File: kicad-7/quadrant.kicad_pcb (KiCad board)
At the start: 4 copper layers, 53 x 73.5 mm, 96 parts, among them J1 USB_C_Receptacle_USB2.0, J2 Conn_01x02_Male, J7 Conn_01x06, Q1 DMN601DMK-7, Q2 NCE3400, U1 VRD2833PTX, U2 W25Q128JVS, U3 VRH4801NTX, U7 DS3911, U8 TSV994IPT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

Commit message: moved component labels
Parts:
- removed C1, C2, C3: 1 uF, Capacitor_SMD:C_0805_2012Metric_Pad1.18x1.45mm_HandSolder
- removed U1: VRD2833PTX, quadrant:SOT-26
- added C25: 1 uF, Capacitor_SMD:C_0805_2012Metric_Pad1.18x1.45mm_HandSolder, F.Cu at (15.5, -50.5)
- added C26: 1 uF, Capacitor_SMD:C_0805_2012Metric_Pad1.18x1.45mm_HandSolder, F.Cu at (7.50, -49.5)
- added C40: 22nF, Capacitor_SMD:C_0805_2012Metric_Pad1.18x1.45mm_HandSolder, F.Cu at (15.5, -48.0)
- added C41: 1 uF, Capacitor_SMD:C_0805_2012Metric_Pad1.18x1.45mm_HandSolder, F.Cu at (7.00, -54.0)
- added C42: 1 uF, Capacitor_SMD:C_0805_2012Metric_Pad1.18x1.45mm_HandSolder, F.Cu at (14.0, -54.0)
- added U4: RT9193-33GB, Package_TO_SOT_SMD:SOT-23-5, F.Cu at (11.0, -49.5)
- added U5: LP5907MFX-2.8_NOPB, Package_TO_SOT_SMD:SOT-23-5, F.Cu at (10.5, -54.0)
- moved MIDI0 4.56 mm to (4.55, -9.22), turned to 180 degrees
- moved VC0 4.55 mm to (4.55, -29.0), turned to 180 degrees
- moved VC3 4.55 mm to (34.5, -4.55), turned to -90 degrees
- moved VC1 4.55 mm to (19.0, -69.0), turned to 90 degrees
- moved VC2 4.45 mm to (48.5, -44.5), turned to 0 degrees
- moved R2 1.70 mm to (3.50, -56.5)
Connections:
- J1 pad A8: Net-(J1-PadA8) -> unconnected-(J1-SBU1-PadA8)
- J1 pad B8: Net-(J1-PadB8) -> unconnected-(J1-SBU2-PadB8)
- MIDI0 pad TN: Net-(MIDI0-PadTN) -> unconnected-(MIDI0-PadTN)
- U3 pad 4: Net-(U3-Pad4) -> unconnected-(U3-NC-Pad4)
- U9 pad 11: Net-(U9-Pad11) -> unconnected-(U9-GPIO8-Pad11)
- U9 pad 12: Net-(U9-Pad12) -> unconnected-(U9-GPIO9-Pad12)
- U9 pad 13: Net-(U9-Pad13) -> unconnected-(U9-GPIO10-Pad13)
- U9 pad 18: Net-(U9-Pad18) -> unconnected-(U9-GPIO15-Pad18)
- U9 pad 19: Net-(U9-Pad19) -> unconnected-(U9-TESTEN-Pad19)
- U9 pad 21: Net-(U9-Pad21) -> unconnected-(U9-XOUT-Pad21)
- U9 pad 26: Net-(U9-Pad26) -> unconnected-(U9-RUN-Pad26)
- U9 pad 27: Net-(U9-Pad27) -> unconnected-(U9-GPIO16-Pad27)
- U9 pad 28: Net-(U9-Pad28) -> unconnected-(U9-GPIO17-Pad28)
- U9 pad 32: Net-(U9-Pad32) -> unconnected-(U9-GPIO21-Pad32)
- U9 pad 34: Net-(U9-Pad34) -> unconnected-(U9-GPIO22-Pad34)
- U9 pad 38: Net-(U9-Pad38) -> unconnected-(U9-GPIO26_ADC0-Pad38)
- U9 pad 39: Net-(U9-Pad39) -> unconnected-(U9-GPIO27_ADC1-Pad39)
- U9 pad 40: Net-(U9-Pad40) -> unconnected-(U9-GPIO28_ADC2-Pad40)
- U9 pad 41: Net-(U9-Pad41) -> unconnected-(U9-GPIO29_ADC3-Pad41)
- U9 pad 5: Net-(U9-Pad5) -> unconnected-(U9-GPIO3-Pad5)
- VC0 pad TN: Net-(VC0-PadTN) -> unconnected-(VC0-PadTN)
- VC1 pad TN: Net-(VC1-PadTN) -> unconnected-(VC1-PadTN)
- VC2 pad TN: Net-(VC2-PadTN) -> unconnected-(VC2-PadTN)
- VC3 pad TN: Net-(VC3-PadTN) -> unconnected-(VC3-PadTN)
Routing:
- net USB5V: track 121.9 -> 134.7 mm
- net +3V3: track 54.3 -> 66.7 mm
- net +2V8: track 103.7 -> 116.1 mm
- net GND: track 87.0 -> 93.6 mm, vias 21 -> 20
- net Net-(U4-BP): track 0.00 -> 2.55 mm
- net Net-(J1-CC2): track 8.34 -> 7.32 mm
- net USBD+: track 36.9 -> 36.1 mm
- net unconnected-(MIDI0-PadTN): vias 0 -> 1
- net SDA: vias 4 -> 3

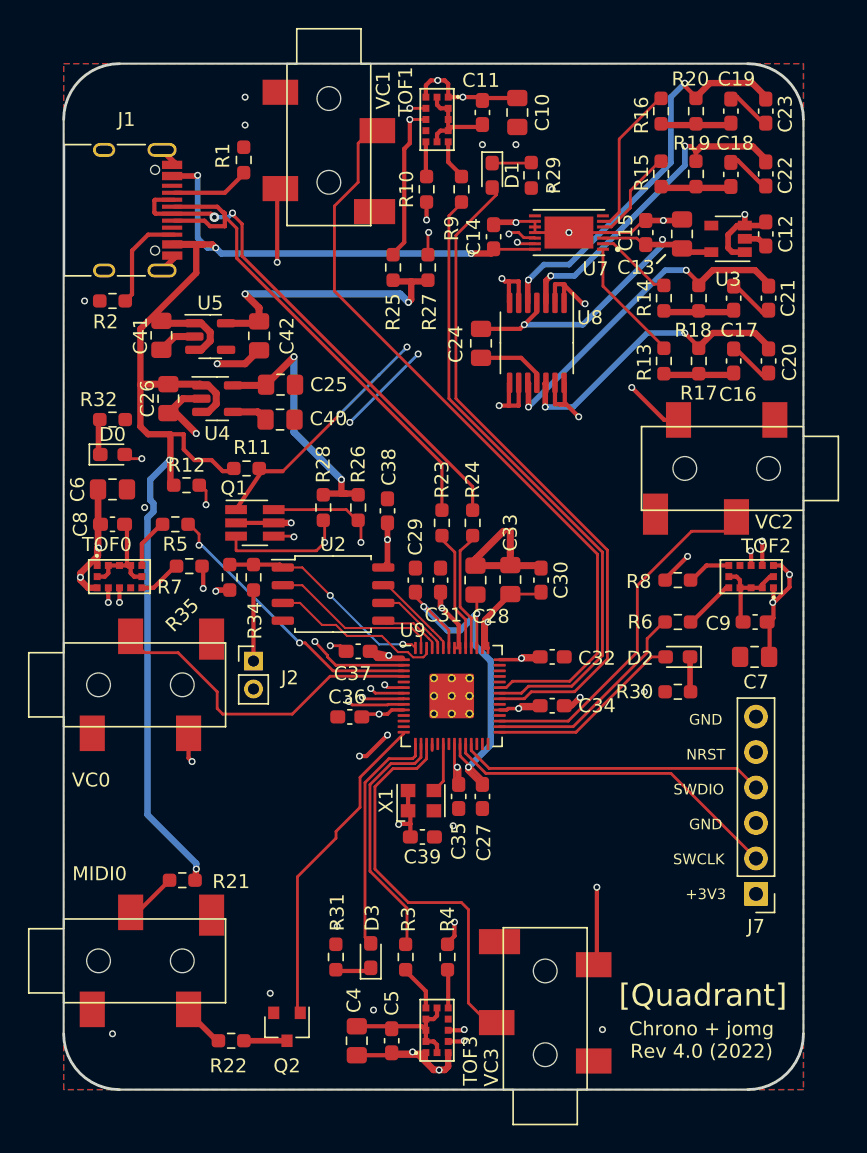
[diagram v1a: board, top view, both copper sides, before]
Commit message: change schottky diode, update pcb
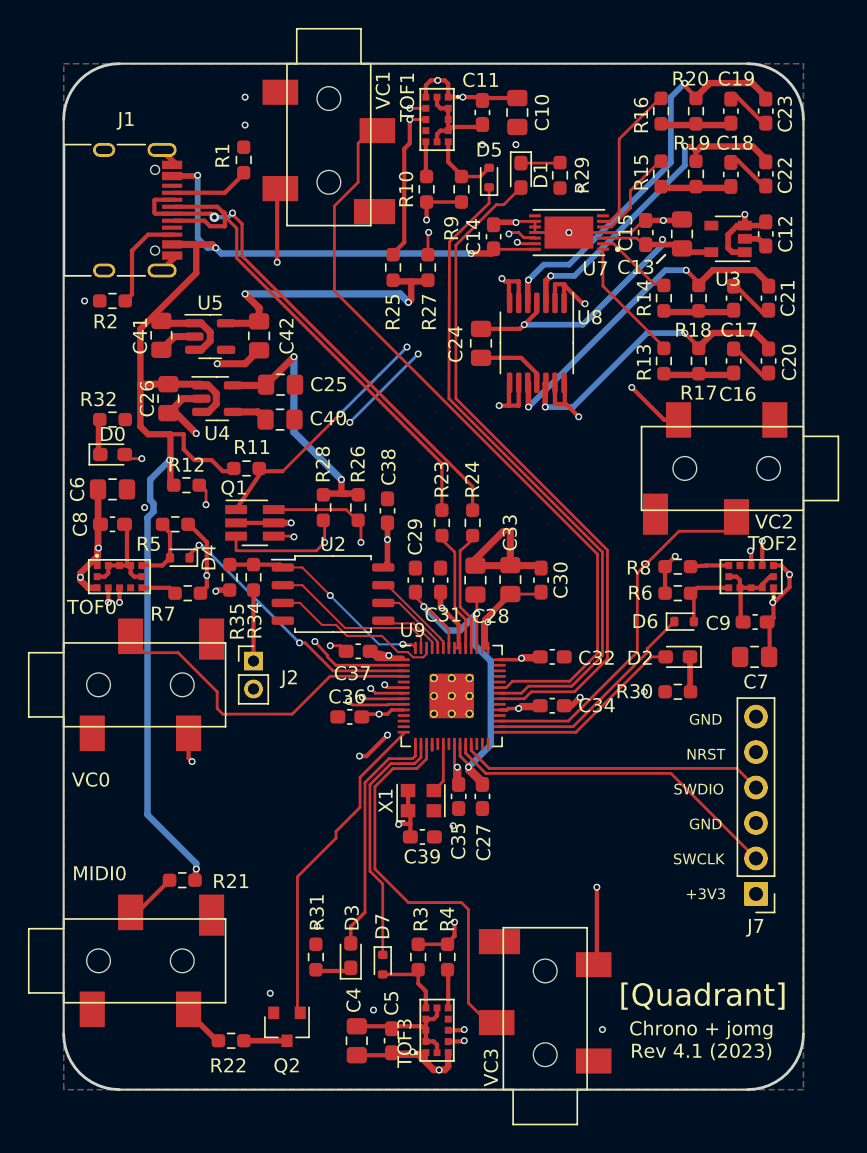
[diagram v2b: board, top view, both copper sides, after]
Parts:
- added D4: D_Schottky, Diode_SMD:D_SOD-523, F.Cu at (8.32, -38.1)
- added D5: D_Schottky, Diode_SMD:D_SOD-523, F.Cu at (30.5, -65.3)
- added D6: D_Schottky, Diode_SMD:D_SOD-523, F.Cu at (44.5, -33.5)
- added D7: D_Schottky, Diode_SMD:D_SOD-523, F.Cu at (22.9, -8.95)
- VC0, VC1, VC2, VC3: value AudioJack2_Ground_SwitchT -> PJ-327C-4A
- moved R29 2.06 mm to (35.6, -65.5)
- moved R6 2.06 mm to (44.0, -35.6)
- moved D1 2.06 mm to (32.8, -65.5)
- moved R7 1.94 mm to (8.89, -35.6)
- moved D3 1.43 mm to (20.6, -9.60)
- moved R31 1.43 mm to (18.1, -9.50)
- moved R8 0.97 mm to (44.0, -37.5)
- moved R3 0.90 mm to (25.4, -9.50)
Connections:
- R3 pad 1: EN3 -> +2V8
- R5 pad 1: EN0 -> +2V8
- R6 pad 1: EN2 -> +2V8
- R9 pad 1: EN1 -> +2V8
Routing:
- net +2V8: track 116.1 -> 125.8 mm
- net Net-(D7-A): track 3.25 -> 5.65 mm
- net Net-(D5-A): track 2.79 -> 5.03 mm
- net EN1: track 45.8 -> 47.8 mm
- net Net-(D6-A): track 3.66 -> 5.14 mm
- net Net-(D4-A): track 3.53 -> 4.90 mm
- net LED1: track 48.4 -> 49.4 mm
- net EN0: track 20.4 -> 19.6 mm
- net GATE2: track 26.0 -> 26.5 mm
- net Net-(TOF0-GPIO1): track 3.04 -> 2.54 mm
- net unconnected-(MIDI0-PadTN): vias 1 -> 0
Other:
- board text added: "Chrono + jomg Rev 4.1 (2023)"
- board text removed: "Chrono + jomg Rev 4.0 (2022)"
